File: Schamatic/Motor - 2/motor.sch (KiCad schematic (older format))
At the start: 50 parts, among them J1 CONN_02X05, J11 V, J12 U, J13 W, J2 RS485, J3 RS485, J6 +BAT, J9 GND, SW1 B3U-1000P, SW2 B3U-1000P, U1 TPS73433DRV, U2 LTC2876, U3 ZXTR2012Z, U4 LM5019, U5 STM32F031K6U6, U6 A1335, U7 IRSM005, U8 IRSM005, U9 IRSM005, Y1 8MhZ

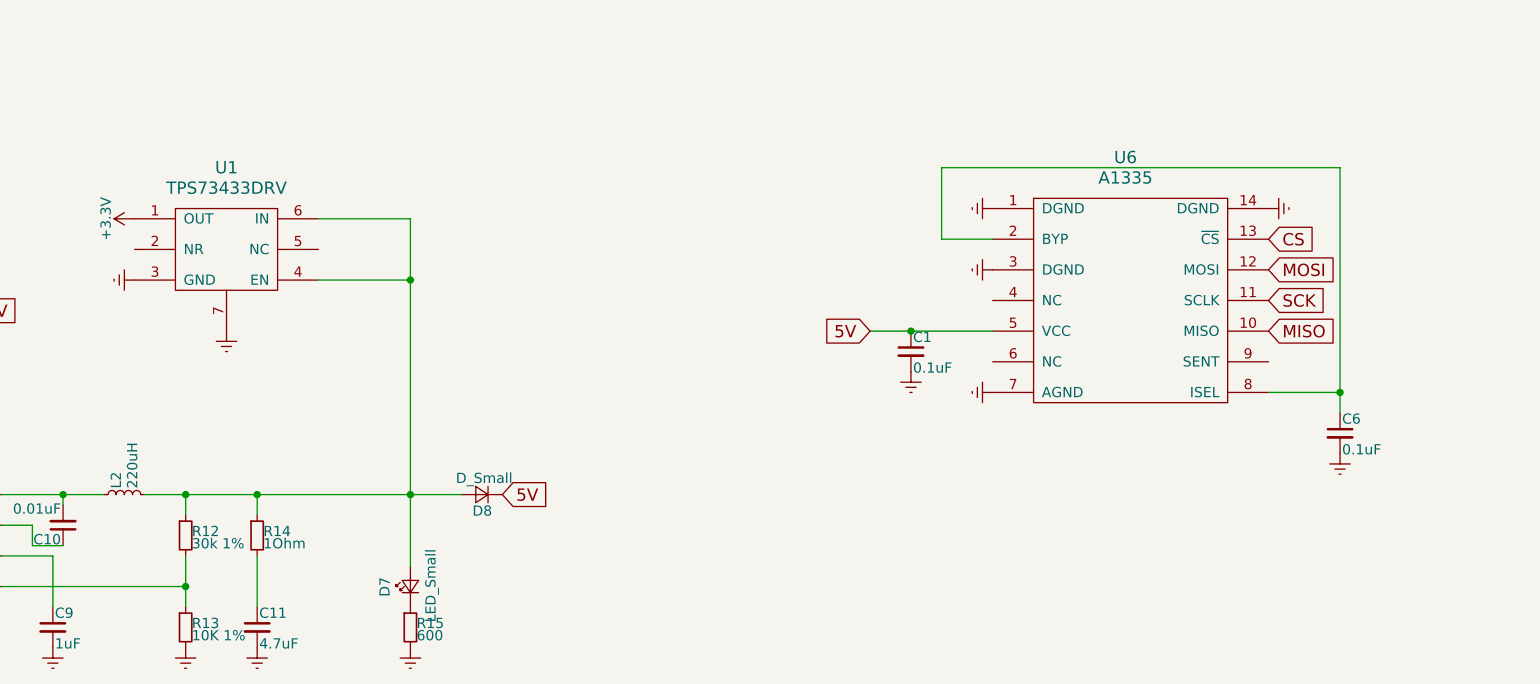
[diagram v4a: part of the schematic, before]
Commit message: problems with A1335 linearization, back to M700
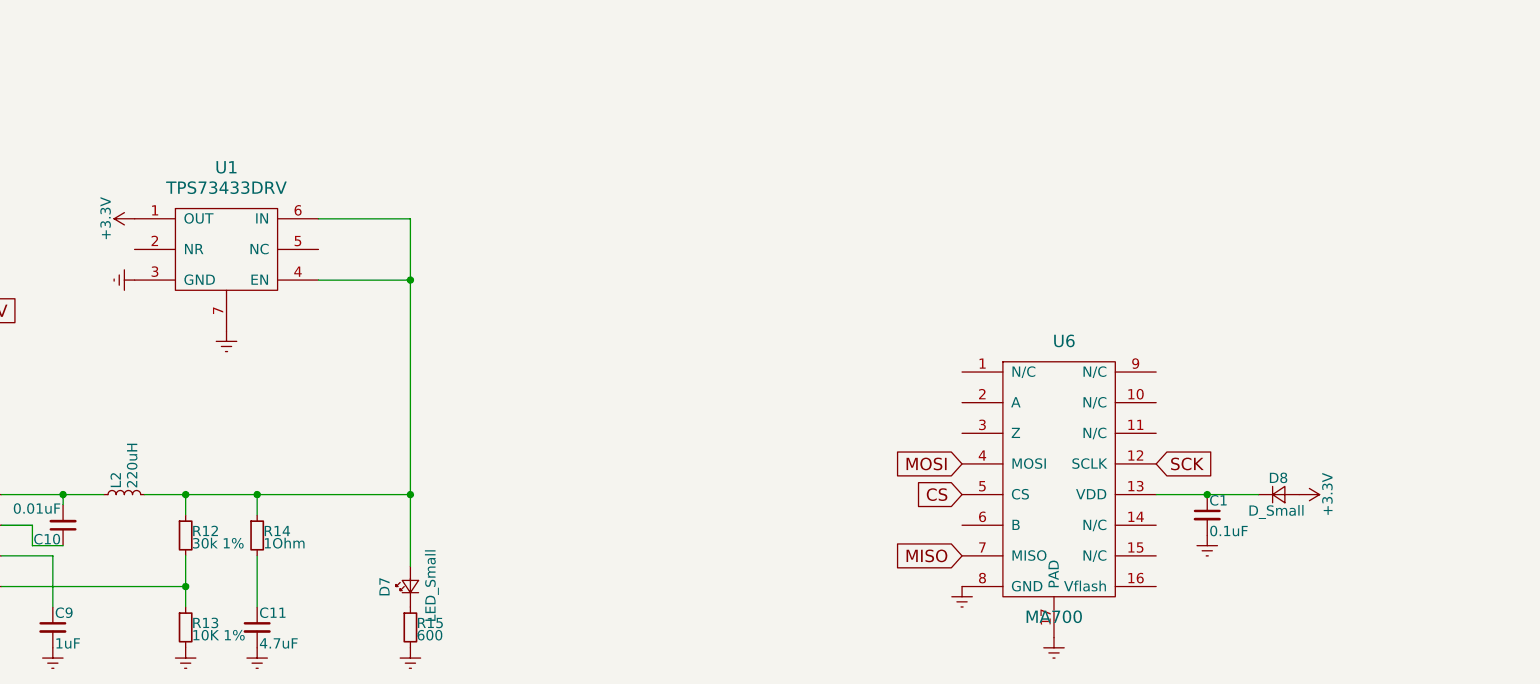
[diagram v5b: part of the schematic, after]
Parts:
- removed C6: 0.1uF, Capacitors_SMD:C_0603, symbol C_Small
- removed U6: A1335, Housings_SSOP:TSSOP-14_4.4x5mm_Pitch0.65mm, symbol A1335
- added U6: MA700, Housings_DFN_QFN:QFN-16-1EP_3x3mm_Pitch0.5mm, symbol MA700
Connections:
- net +3V3: now also D8.2 (A)
- net CS: now also U6.5 (CS)
- net Earth: now also U6.17 (PAD), U6.8 (GND)
- net MISO: now also U6.7 (MISO)
- net MOSI: now also U6.4 (MOSI)
- net SCK: now also U6.12 (SCLK)
- net at D7.2 (A), L2.2, R12.1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: no longer D8.2 (A)
- net 5V: no longer names the net of C1.1, D8.1 (K)
- net 5V: now also U6.13 (VDD)
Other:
- moved on the sheet: D8
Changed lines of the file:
@@
 $EndDescr
 $Comp
-L Earth #PWR44
+L Earth #PWR42
 U 1 1 59775888
 P 11200 2150
-F 0 "#PWR44" H 11200 1900 50  0001 C CNN
+F 0 "#PWR42" H 11200 1900 50  0001 C CNN
 F 1 "Earth" H 11200 2000 50  0001 C CNN
 F 2 "" H 11200 2150 50  0001 C CNN
@@
 NRST
 $Comp
-L Earth #PWR45
+L Earth #PWR43
 U 1 1 59785376
 P 11200 4450
-F 0 "#PWR45" H 11200 4200 50  0001 C CNN
+F 0 "#PWR43" H 11200 4200 50  0001 C CNN
 F 1 "Earth" H 11200 4300 50  0001 C CNN
 F 2 "" H 11200 4450 50  0001 C CNN
@@
 $EndComp
 $Comp
-L Earth #PWR46
+L Earth #PWR44
 U 1 1 59785504
 P 11200 7100
-F 0 "#PWR46" H 11200 6850 50  0001 C CNN
+F 0 "#PWR44" H 11200 6850 50  0001 C CNN
 F 1 "Earth" H 11200 6950 50  0001 C CNN
 F 2 "" H 11200 7100 50  0001 C CNN
@@
 	2750 8400 3250 8400
 Wire Wire Line
-	3450 8400 5000 8400
-Wire Wire Line
 	3050 8450 3050 8400
 Connection ~ 3050 8400
@@
 Connection ~ 3650 8850
 Wire Wire Line
-	4000 8500 4000 8400
+	4000 8400 4000 8500
 Connection ~ 4000 8400
 Wire Wire Line
@@
 $EndComp
 $Comp
-L +BATT #PWR47
+L +BATT #PWR45
 U 1 1 5B1C2E23
 P 12650 950
-F 0 "#PWR47" H 12650 800 50  0001 C CNN
+F 0 "#PWR45" H 12650 800 50  0001 C CNN
 F 1 "+BATT" H 12650 1090 50  0000 C CNN
 F 2 "" H 12650 950 50  0001 C CNN
@@
 $EndComp
 $Comp
-L +BATT #PWR49
+L +BATT #PWR47
 U 1 1 5B1C30B2
 P 12650 3200
-F 0 "#PWR49" H 12650 3050 50  0001 C CNN
+F 0 "#PWR47" H 12650 3050 50  0001 C CNN
 F 1 "+BATT" H 12650 3340 50  0000 C CNN
 F 2 "" H 12650 3200 50  0001 C CNN
@@
 $EndComp
 $Comp
-L +BATT #PWR51
+L +BATT #PWR49
 U 1 1 5B1C3147
 P 12650 5800
-F 0 "#PWR51" H 12650 5650 50  0001 C CNN
+F 0 "#PWR49" H 12650 5650 50  0001 C CNN
 F 1 "+BATT" H 12650 5940 50  0000 C CNN
 F 2 "" H 12650 5800 50  0001 C CNN
@@
 $EndComp
 $Comp
-L C_Small C1
-U 1 1 5B35926B
-P 7200 7700
-F 0 "C1" H 7210 7770 50  0000 L CNN
-F 1 "0.1uF" H 7210 7620 50  0000 L CNN
-F 2 "Capacitors_SMD:C_0603" H 7200 7700 50  0001 C CNN
-F 3 "" H 7200 7700 50  0001 C CNN
-	1    7200 7700
-	1    0    0    -1
-$EndComp
-$Comp
-L Earth #PWR38
-U 1 1 5B35AFE4
-P 7200 7800
-F 0 "#PWR38" H 7200 7550 50  0001 C CNN
-F 1 "Earth" H 7200 7650 50  0001 C CNN
-F 2 "" H 7200 7800 50  0001 C CNN
-F 3 "" H 7200 7800 50  0001 C CNN
-	1    7200 7800
-	1    0    0    -1
-$EndComp
-Text GLabel 8950 7150 2    60   Input ~ 0
-CS
-Text GLabel 8950 7450 2    60   Input ~ 0
-SCK
-Text GLabel 8950 7300 2    60   Input ~ 0
-MOSI
-$Comp
-L Earth #PWR42
-U 1 1 5B361612
-P 8950 7000
-F 0 "#PWR42" H 8950 6750 50  0001 C CNN
-F 1 "Earth" H 8950 6850 50  0001 C CNN
-F 2 "" H 8950 7000 50  0001 C CNN
-F 3 "" H 8950 7000 50  0001 C CNN
-	1    8950 7000
-	0    -1   -1   0
-$EndComp
-$Comp
 L Earth #PWR25
 U 1 1 5B362B44
@@
 	0    1    1    0
 $EndComp
-Text GLabel 8950 7600 2    60   Input ~ 0
-MISO
 $Comp
 L IRSM005 U7
@@
 Connection ~ 11200 1950
 $Comp
-L Earth #PWR48
+L Earth #PWR46
 U 1 1 5B508DF7
 P 12650 2300
-F 0 "#PWR48" H 12650 2050 50  0001 C CNN
+F 0 "#PWR46" H 12650 2050 50  0001 C CNN
 F 1 "Earth" H 12650 2150 50  0001 C CNN
 F 2 "" H 12650 2300 50  0001 C CNN
@@
 Connection ~ 11200 6850
 $Comp
-L Earth #PWR52
+L Earth #PWR50
 U 1 1 5B51C6EC
 P 12650 7200
-F 0 "#PWR52" H 12650 6950 50  0001 C CNN
+F 0 "#PWR50" H 12650 6950 50  0001 C CNN
 F 1 "Earth" H 12650 7050 50  0001 C CNN
 F 2 "" H 12650 7200 50  0001 C CNN
@@
 Connection ~ 11200 6350
 $Comp
-L A1335 U6
-U 1 1 5B52BFBF
-P 8250 6850
-F 0 "U6" H 8250 6950 60  0000 C CNN
-F 1 "A1335" H 8250 6850 60  0000 C CNN
-F 2 "Housings_SSOP:TSSOP-14_4.4x5mm_Pitch0.65mm" H 8250 6850 60  0001 C CNN
-F 3 "" H 8250 6850 60  0001 C CNN
-	1    8250 6850
-	1    0    0    -1
-$EndComp
-$Comp
-L Earth #PWR39
-U 1 1 5B52D619
-P 7600 7000
-F 0 "#PWR39" H 7600 6750 50  0001 C CNN
-F 1 "Earth" H 7600 6850 50  0001 C CNN
-F 2 "" H 7600 7000 50  0001 C CNN
-F 3 "" H 7600 7000 50  0001 C CNN
-	1    7600 7000
-	0    1    1    0
-$EndComp
-$Comp
-L Earth #PWR40
-U 1 1 5B52D6C3
-P 7600 7300
-F 0 "#PWR40" H 7600 7050 50  0001 C CNN
-F 1 "Earth" H 7600 7150 50  0001 C CNN
-F 2 "" H 7600 7300 50  0001 C CNN
-F 3 "" H 7600 7300 50  0001 C CNN
-	1    7600 7300
-	0    1    1    0
-$EndComp
-$Comp
-L Earth #PWR41
-U 1 1 5B52D76D
-P 7600 7900
-F 0 "#PWR41" H 7600 7650 50  0001 C CNN
-F 1 "Earth" H 7600 7750 50  0001 C CNN
-F 2 "" H 7600 7900 50  0001 C CNN
-F 3 "" H 7600 7900 50  0001 C CNN
-	1    7600 7900
-	0    1    1    0
-$EndComp
-$Comp
 L D_Small D8
 U 1 1 5B52EBF3
-P 5100 8400
-F 0 "D8" H 5050 8480 50  0000 L CNN
-F 1 "D_Small" H 4950 8320 50  0000 L CNN
-F 2 "Diodes_SMD:D_SOD-323F" V 5100 8400 50  0001 C CNN
-F 3 "" V 5100 8400 50  0001 C CNN
-	1    5100 8400
-	-1   0    0    1
-$EndComp
-Text GLabel 5200 8400 2    60   Input ~ 0
-5V
-Text GLabel 7000 7600 0    60   Input ~ 0
-5V
-Wire Wire Line
-	7000 7600 7600 7600
-Connection ~ 7200 7600
-Wire Wire Line
-	8950 7900 9300 7900
-Wire Wire Line
-	9300 6800 9300 8000
-Wire Wire Line
-	9300 6800 7350 6800
-Wire Wire Line
-	7350 6800 7350 7150
-Wire Wire Line
-	7350 7150 7600 7150
-$Comp
-L C_Small C6
-U 1 1 5B5300E5
-P 9300 8100
-F 0 "C6" H 9310 8170 50  0000 L CNN
-F 1 "0.1uF" H 9310 8020 50  0000 L CNN
-F 2 "Capacitors_SMD:C_0603" H 9300 8100 50  0001 C CNN
-F 3 "" H 9300 8100 50  0001 C CNN
-	1    9300 8100
-	1    0    0    -1
-$EndComp
-$Comp
-L Earth #PWR43
-U 1 1 5B5301C3
-P 9300 8200
-F 0 "#PWR43" H 9300 7950 50  0001 C CNN
-F 1 "Earth" H 9300 8050 50  0001 C CNN
-F 2 "" H 9300 8200 50  0001 C CNN
-F 3 "" H 9300 8200 50  0001 C CNN
-	1    9300 8200
-	1    0    0    -1
-$EndComp
-Connection ~ 9300 7900
+P 9000 8400
+F 0 "D8" H 8950 8480 50  0000 L CNN
+F 1 "D_Small" H 8850 8320 50  0000 L CNN
+F 2 "Diodes_SMD:D_SOD-323F" V 9000 8400 50  0001 C CNN
+F 3 "" V 9000 8400 50  0001 C CNN
+	1    9000 8400
+	1    0    0    -1
+$EndComp
 Wire Wire Line
 	12950 1650 12950 1600
@@
 	12000 7200 12150 7200
 $Comp
-L Earth #PWR50
+L Earth #PWR48
 U 1 1 5B52FE10
 P 12650 4600
-F 0 "#PWR50" H 12650 4350 50  0001 C CNN
+F 0 "#PWR48" H 12650 4350 50  0001 C CNN
 F 1 "Earth" H 12650 4450 50  0001 C CNN
 F 2 "" H 12650 4600 50  0001 C CNN
@@
 Text GLabel 1100 2600 2    60   Input ~ 0
 RS-B
+$Comp
+L MA700 U6
+U 1 1 5B781547
+P 7950 8600
+F 0 "U6" H 7950 9550 60  0000 C CNN
+F 1 "MA700" H 7900 8200 60  0000 C CNN
+F 2 "Housings_DFN_QFN:QFN-16-1EP_3x3mm_Pitch0.5mm" H 7950 8600 60  0001 C CNN
+F 3 "" H 7950 8600 60  0001 C CNN
+	1    7950 8600
+	1    0    0    -1
+$EndComp
+$Comp
+L C_Small C1
+U 1 1 5B782F56
+P 8650 8500
+F 0 "C1" H 8660 8570 50  0000 L CNN
+F 1 "0.1uF" H 8660 8420 50  0000 L CNN
+F 2 "Capacitors_SMD:C_0603" H 8650 8500 50  0001 C CNN
+F 3 "" H 8650 8500 50  0001 C CNN
+	1    8650 8500
+	1    0    0    -1
+$EndComp
+Wire Wire Line
+	8400 8400 8900 8400
+Connection ~ 8650 8400
+$Comp
+L Earth #PWR40
+U 1 1 5B784055
+P 8650 8600
+F 0 "#PWR40" H 8650 8350 50  0001 C CNN
+F 1 "Earth" H 8650 8450 50  0001 C CNN
+F 2 "" H 8650 8600 50  0001 C CNN
+F 3 "" H 8650 8600 50  0001 C CNN
+	1    8650 8600
+	1    0    0    -1
+$EndComp
+$Comp
+L Earth #PWR39
+U 1 1 5B784A54
+P 7900 9100
+F 0 "#PWR39" H 7900 8850 50  0001 C CNN
+F 1 "Earth" H 7900 8950 50  0001 C CNN
+F 2 "" H 7900 9100 50  0001 C CNN
+F 3 "" H 7900 9100 50  0001 C CNN
+	1    7900 9100
+	1    0    0    -1
+$EndComp
+$Comp
+L Earth #PWR38
+U 1 1 5B7853C0
+P 7450 8850
+F 0 "#PWR38" H 7450 8600 50  0001 C CNN
+F 1 "Earth" H 7450 8700 50  0001 C CNN
+F 2 "" H 7450 8850 50  0001 C CNN
+F 3 "" H 7450 8850 50  0001 C CNN
+	1    7450 8850
+	1    0    0    -1
+$EndComp
+Wire Wire Line
+	3450 8400 4750 8400
+$Comp
+L +3.3V #PWR41
+U 1 1 5B785E48
+P 9100 8400
+F 0 "#PWR41" H 9100 8250 50  0001 C CNN
+F 1 "+3.3V" H 9100 8540 50  0000 C CNN
+F 2 "" H 9100 8400 50  0001 C CNN
+F 3 "" H 9100 8400 50  0001 C CNN
+	1    9100 8400
+	0    1    1    0
+$EndComp
+Text GLabel 7450 8700 0    60   Input ~ 0
+MISO
+Text GLabel 7450 8400 0    60   Input ~ 0
+CS
+Text GLabel 8400 8250 2    60   Input ~ 0
+SCK
+Text GLabel 7450 8250 0    60   Input ~ 0
+MOSI
 $EndSCHEMATC
